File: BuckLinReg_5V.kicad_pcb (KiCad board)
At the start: 2 copper layers, 96 x 56 mm, 41 parts, among them J1 Barrel_Jack, J2 Conn_01x02_Male, J3 Conn_01x02_Male, J4 Conn_01x02_Male, Q1 SQD40061EL, U1 TPS56339DDC, U2 LM1085-5.0

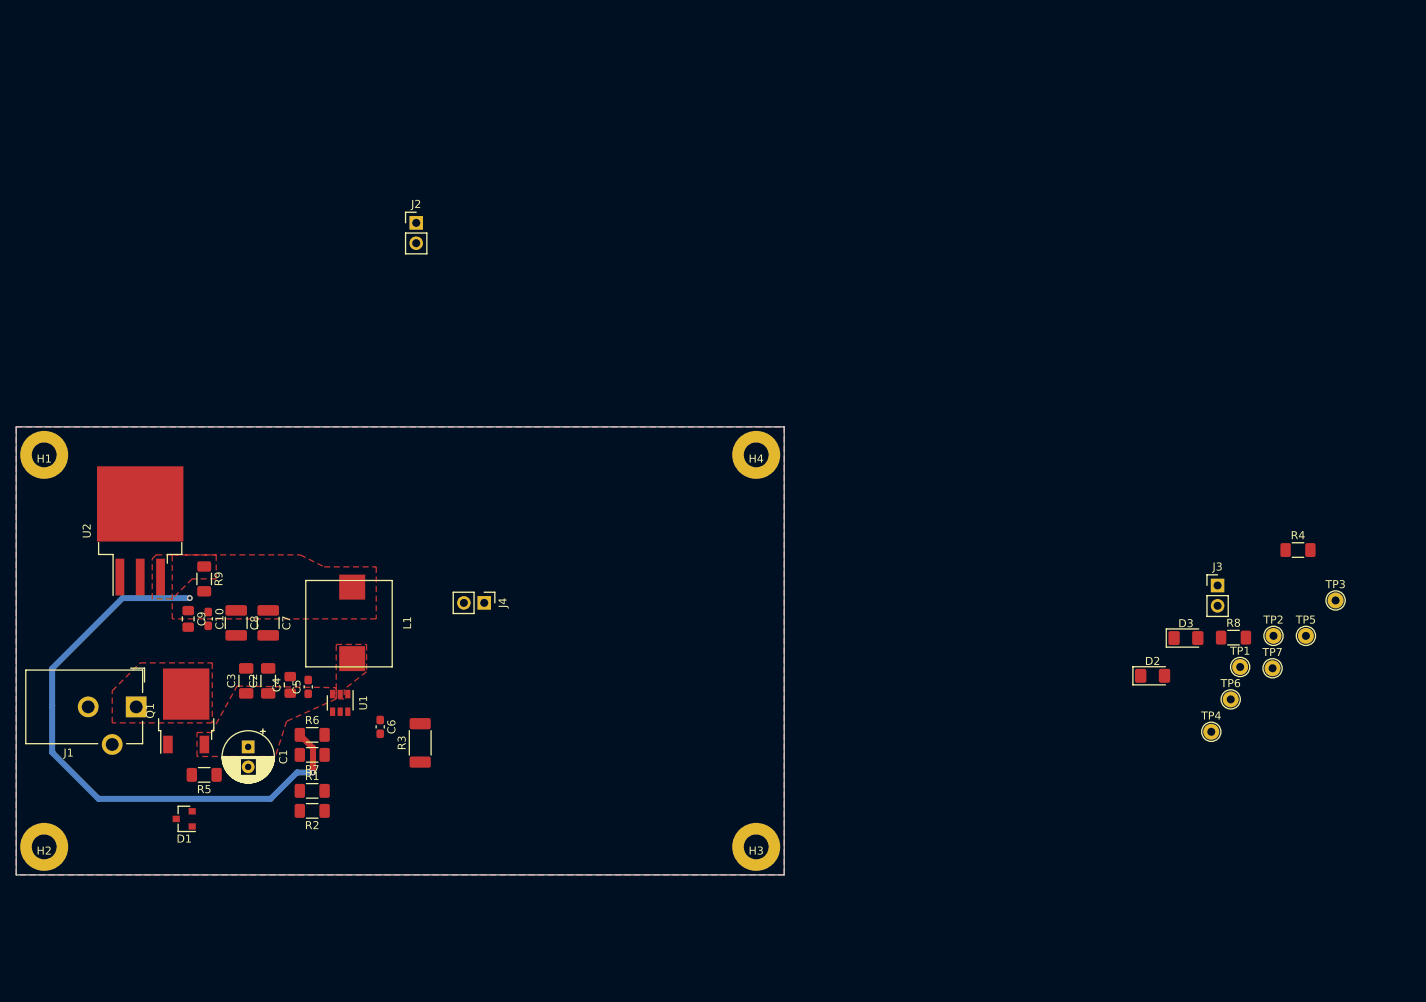
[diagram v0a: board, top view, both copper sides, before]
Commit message: Added overcurrent protection circuit and assigned all MFPNs and footprints
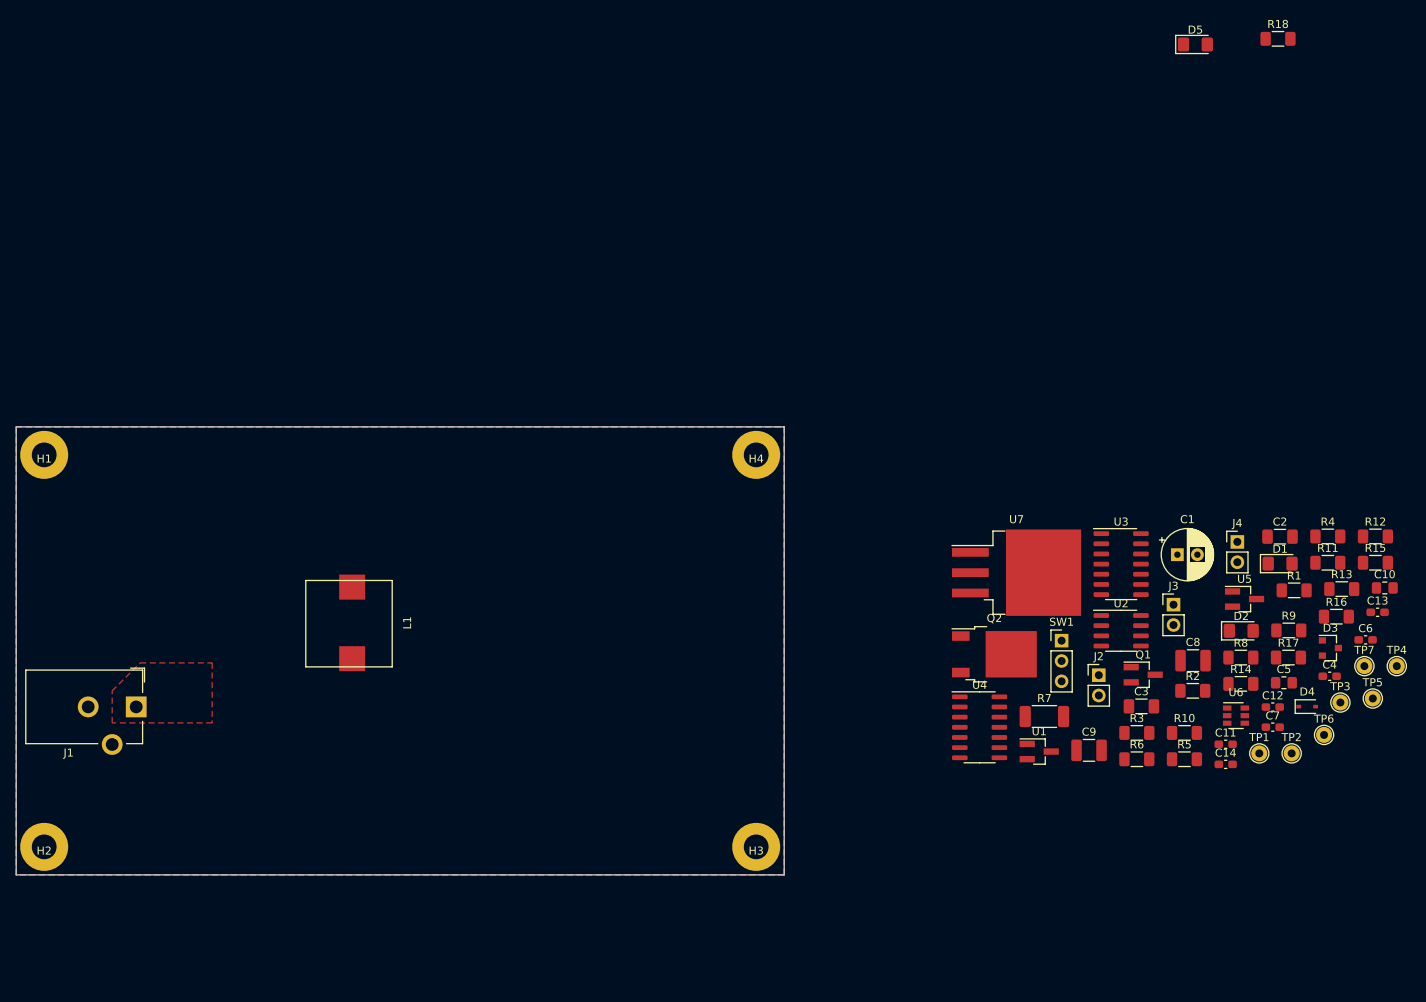
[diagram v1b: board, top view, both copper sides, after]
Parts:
- added C11: 0.1u, Capacitor_SMD:C_0603_1608Metric_Pad1.08x0.95mm_HandSolder, F.Cu at (209.2, 91.7)
- added C12: 0.1u, Capacitor_SMD:C_0603_1608Metric_Pad1.08x0.95mm_HandSolder, F.Cu at (215.1, 87.0)
- added C13: 0.1u, Capacitor_SMD:C_0603_1608Metric_Pad1.08x0.95mm_HandSolder, F.Cu at (228.2, 75.2)
- added C14: 0.1u, Capacitor_SMD:C_0603_1608Metric_Pad1.08x0.95mm_HandSolder, F.Cu at (209.2, 94.2)
- added D4: 3.0, Diode_SMD:D_SOD-323, F.Cu at (219.4, 87.0)
- added D5: YELLOW, Diode_SMD:D_1206_3216Metric_Pad1.42x1.75mm_HandSolder, F.Cu at (205.4, 4.20)
- added Q2: SQD40061EL, Package_TO_SOT_SMD:TO-252-2, F.Cu at (180.3, 80.4)
- added R10: 10k, Resistor_SMD:R_1206_3216Metric_Pad1.30x1.75mm_HandSolder, F.Cu at (204.0, 90.3)
- added R11: 1k, Resistor_SMD:R_1206_3216Metric_Pad1.30x1.75mm_HandSolder, F.Cu at (222.0, 69.0)
- added R12: 1k, Resistor_SMD:R_1206_3216Metric_Pad1.30x1.75mm_HandSolder, F.Cu at (227.9, 65.7)
- added R13: 100k, Resistor_SMD:R_1206_3216Metric_Pad1.30x1.75mm_HandSolder, F.Cu at (223.7, 72.3)
- added R14: 100k, Resistor_SMD:R_1206_3216Metric_Pad1.30x1.75mm_HandSolder, F.Cu at (211.1, 84.1)
- added R15: 10m, Resistor_SMD:R_1206_3216Metric_Pad1.30x1.75mm_HandSolder, F.Cu at (227.9, 69.0)
- added R16: 100k, Resistor_SMD:R_1206_3216Metric_Pad1.30x1.75mm_HandSolder, F.Cu at (223.0, 75.7)
- added R17: 12k, Resistor_SMD:R_1206_3216Metric_Pad1.30x1.75mm_HandSolder, F.Cu at (217.0, 80.8)
- added R18: 10k, Resistor_SMD:R_1206_3216Metric_Pad1.30x1.75mm_HandSolder, F.Cu at (215.7, 3.50)
- added SW1: SW_SPDT, Connector_PinHeader_2.54mm:PinHeader_1x03_P2.54mm_Vertical, F.Cu at (188.7, 78.7)
- added U3: 74HCT00, Package_SO:SOIC-14_3.9x8.7mm_P1.27mm, F.Cu at (196.1, 69.2)
- added U4: SN74HCT02, Package_SO:SOIC-14_3.9x8.7mm_P1.27mm, F.Cu at (178.4, 89.6)
- added U5: TCM810, Package_TO_SOT_SMD:SOT-23_Handsoldering, F.Cu at (211.5, 73.5)
- added U6: TPS56339DDC, Package_TO_SOT_SMD:SOT-23-6, F.Cu at (210.5, 88.1)
- added U7: LM1084-5.0, Package_TO_SOT_SMD:TO-263-3_TabPin2, F.Cu at (183.0, 70.2)
- C10, C5: footprint Capacitor_SMD:C_0603_1608Metric_Pad1.08x0.95mm_HandSolder -> Capacitor_SMD:C_0805_2012Metric_Pad1.18x1.45mm_HandSolder
- C4: footprint Capacitor_SMD:C_0805_2012Metric_Pad1.18x1.45mm_HandSolder -> Capacitor_SMD:C_0603_1608Metric_Pad1.08x0.95mm_HandSolder
- C7: value 10u -> 0.1u; footprint Capacitor_SMD:C_1210_3225Metric_Pad1.33x2.70mm_HandSolder -> Capacitor_SMD:C_0603_1608Metric_Pad1.08x0.95mm_HandSolder
- C9: value 0.1u -> 10u; footprint Capacitor_SMD:C_0805_2012Metric_Pad1.18x1.45mm_HandSolder -> Capacitor_SMD:C_1210_3225Metric_Pad1.33x2.70mm_HandSolder
- D1: value 10V -> GREEN; footprint Diode_SMD:D_SOT-23_ANK -> Diode_SMD:D_1206_3216Metric_Pad1.42x1.75mm_HandSolder
- D3: value GREEN -> 10V; footprint Diode_SMD:D_1206_3216Metric_Pad1.42x1.75mm_HandSolder -> Diode_SMD:D_SOT-23_ANK
- J2, J3, J4: value Conn_01x02_Male -> 1x2 Male
- Q1: value SQD40061EL -> PMBT2222; footprint Package_TO_SOT_SMD:TO-252-2 -> Package_TO_SOT_SMD:SOT-23_Handsoldering
- R1: value 22.1k -> 10k
- R2: value 3.6k -> 10k
- R3: value 30 -> 22.1k; footprint Resistor_SMD:R_2010_5025Metric_Pad1.40x2.65mm_HandSolder -> Resistor_SMD:R_1206_3216Metric_Pad1.30x1.75mm_HandSolder
- R4: value 10k -> 3.6k
- R6: value 36k -> 10k
- R7: value 4.7k -> 30; footprint Resistor_SMD:R_1206_3216Metric_Pad1.30x1.75mm_HandSolder -> Resistor_SMD:R_2010_5025Metric_Pad1.40x2.65mm_HandSolder
- R8: value 10k -> 68k
- R9: value 10m -> 33k
- TP1: value Vin -> U1Vin
- TP2: value U1Vin -> EN
- TP3: value EN -> Vin
- U1: value TPS56339DDC -> TLV76050DBZT; footprint Package_TO_SOT_SMD:SOT-23-6 -> Package_TO_SOT_SMD:SOT-23_Handsoldering
- U2: value LM1085-5.0 -> LMV358; footprint Package_TO_SOT_SMD:TO-263-3_TabPin2 -> Package_SO:SOIC-8_3.9x4.9mm_P1.27mm
- moved C10 147.1 mm to (229.1, 72.1), turned to 0 degrees
- moved D1 140.7 mm to (216.0, 69.1), turned to 0 degrees
- moved R9 135.7 mm to (217.1, 77.4), turned to 0 degrees
- moved C4 129.9 mm to (222.2, 83.2), turned to 0 degrees
- moved C2 127.8 mm to (216.0, 65.7), turned to 0 degrees
- moved C7 126.2 mm to (215.1, 89.5), turned to 0 degrees
- moved R1 125.3 mm to (217.7, 72.4)
- moved C6 123.7 mm to (226.7, 78.6), turned to 0 degrees
- moved U2 123.2 mm to (196.1, 77.5), turned to 0 degrees
- moved R5 122.6 mm to (204.0, 93.5), turned to 0 degrees
- moved C5 122.0 mm to (216.5, 84.0), turned to 0 degrees
- moved Q1 119.7 mm to (198.9, 83.0), turned to 0 degrees
- moved C8 119.7 mm to (205.1, 81.2), turned to 0 degrees
- moved C1 118.6 mm to (203.2, 68.0), turned to 0 degrees
- moved C9 113.8 mm to (192.1, 92.4), turned to 0 degrees
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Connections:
- C1 pad 1: /U1Vin -> /+Vin
- C10 pad 1: /CapNode -> /SR+
- C2 pad 1: /U1Vin -> /+Vin
- C3 pad 1: /U1Vin -> /+Vin
- C4 pad 1: /U1Vin -> /5V0_LOGIC
- C5 pad 1: /U1Vin -> /+Vin
- C6 pad 1: /BOOT -> /+Vin
- C6 pad 2: Net-(C6-Pad2) -> GND
- C7 pad 1: /CapNode -> /BOOT
- C7 pad 2: GND -> Net-(C7-Pad2)
- C8 pad 1: /CapNode -> /SR+
- C9 pad 1: /CapNode -> /SR+
- D1 pad 1: /U1Vin -> GND
- D1 pad 2: /PCheckG -> Net-(D1-Pad2)
- D3 pad 1: GND -> /+Vin
- D3 pad 2: Net-(D3-Pad2) -> /PCheckG
- J2 pad 2: /Vout -> /SR+
- J3 pad 1: GND -> /SR-
- J3 pad 2: /CapNode -> /SR+
- J4 pad 1: /U2Vin -> GND
- J4 pad 2: /CapNode -> /5V0_Out
- L1 pad 2: /CapNode -> /SR+
- Q1 pad 1: /PCheckG -> Net-(Q1-Pad1)
- Q1 pad 2: /Vin -> GND
- Q1 pad 3: /U1Vin -> /EN
- R1 pad 1: /U1Vin -> Net-(D1-Pad2)
- R1 pad 2: /EN -> /+Vin
- R2 pad 1: /EN -> /~PWR_EN
- R2 pad 2: GND -> Net-(Q1-Pad1)
- R3 pad 1: Net-(C6-Pad2) -> /+Vin
- R3 pad 2: /SW -> /EN
- R4 pad 1: Net-(D2-Pad2) -> /EN
- R5 pad 1: /PCheckG -> Net-(D2-Pad2)
- R6 pad 1: /CapNode -> /PCheckG
- R6 pad 2: /FB -> GND
- R7 pad 1: /FB -> Net-(C7-Pad2)
- R7 pad 2: GND -> /SW
- R8 pad 1: Net-(D3-Pad2) -> /SR+
- R8 pad 2: /U1Vin -> /FB
- R9 pad 1: /U2Vin -> /FB
- R9 pad 2: /CapNode -> GND
- TP1 pad 1: /Vin -> /+Vin
- TP2 pad 1: /U1Vin -> /EN
- TP3 pad 1: /EN -> /Vin
- TP7 pad 1: /CapNode -> /SR+
- U1 pad 1: GND -> /5V0_LOGIC
- U1 pad 2: /SW -> /+Vin
- U1 pad 3: /U1Vin -> GND
- U2 pad 1: GND -> /Vo
- U2 pad 2: /Vout -> Net-(R11-Pad1)
- U2 pad 3: /U2Vin -> Net-(R12-Pad1)
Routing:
- net /CapNode: track 73.1 -> 0.00 mm, vias 2 -> 0
- removed copper zone on F.Cu, net /CapNode
- removed copper zone on F.Cu, net /SW
- removed copper zone on F.Cu, net /U1Vin
- removed copper zone on F.Cu, net /U2Vin

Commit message: Two grounds: GNDA and pwrGND.  Continued PCB dev.
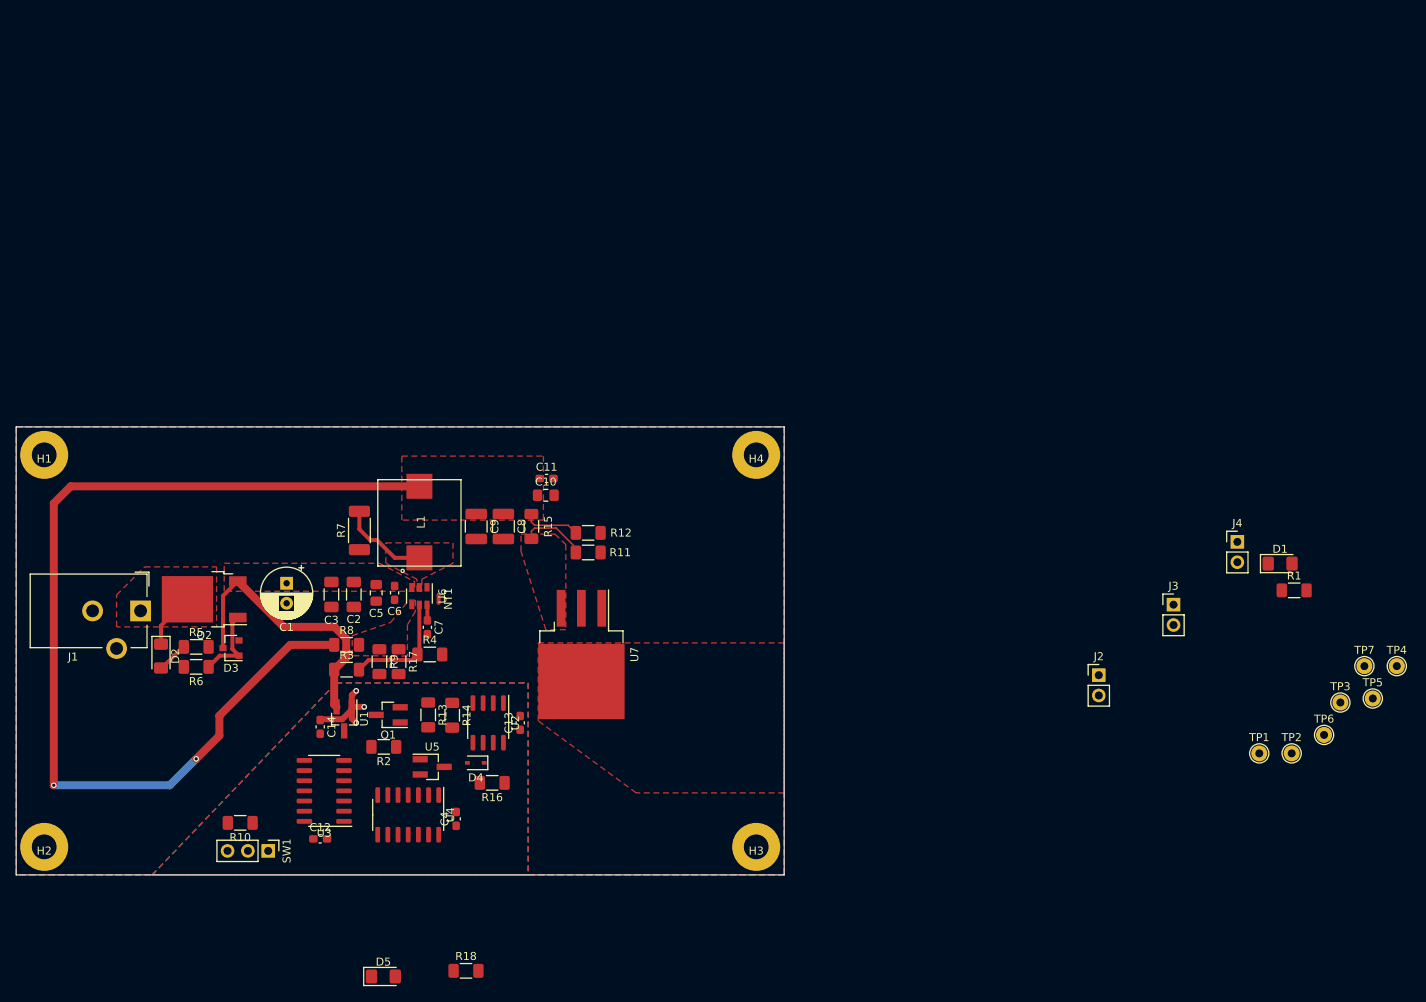
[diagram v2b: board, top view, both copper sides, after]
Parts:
- added NT1: Net-Tie_2, NetTie:NetTie-2_SMD_Pad0.5mm, F.Cu at (110.8, 73.5)
- moved D5 154.5 mm to (103.9, 120.7)
- moved R18 154.5 mm to (114.2, 120.0)
- moved D3 137.4 mm to (84.8, 79.7), turned to 180 degrees
- moved D2 135.1 mm to (76.1, 80.7), turned to 270 degrees
- moved R5 124.3 mm to (80.5, 79.5)
- moved C6 121.5 mm to (105.3, 72.8), turned to 270 degrees
- moved C12 120.2 mm to (96.0, 103.5)
- moved R10 118.6 mm to (86.0, 101.5), turned to 180 degrees
- moved R6 118.2 mm to (80.5, 82.0), turned to 180 degrees
- moved C2 116.0 mm to (100.2, 73.0), turned to 270 degrees
- moved R13 115.3 mm to (109.5, 88.0), turned to 270 degrees
- moved C5 114.0 mm to (103.0, 72.8), turned to 270 degrees
- moved R9 113.7 mm to (103.4, 81.3), turned to 270 degrees
- moved C14 113.3 mm to (96.0, 89.5), turned to 270 degrees
- moved R4 113.2 mm to (109.7, 80.5)
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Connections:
- net Net-(R11-Pad1) renamed /DFA-
- net Net-(R12-Pad1) renamed /DFA+
- C1 pad 2: GND -> GNDPWR
- C10 pad 2: GND -> GNDPWR
- C11 pad 2: GND -> GNDPWR
- C12 pad 2: GND -> GNDA
- C13 pad 2: GND -> GNDA
- C14 pad 2: GND -> GNDA
- C2 pad 2: GND -> GNDPWR
- C3 pad 2: GND -> GNDPWR
- C4 pad 2: GND -> GNDA
- C5 pad 2: GND -> GNDPWR
- C6 pad 2: GND -> GNDPWR
- C8 pad 2: GND -> GNDPWR
- C9 pad 2: GND -> GNDPWR
- D1 pad 1: GND -> GNDPWR
- D4 pad 2: GND -> GNDA
- H1 pad 1: GND -> GNDPWR
- H2 pad 1: GND -> GNDPWR
- H3 pad 1: GND -> GNDPWR
- H4 pad 1: GND -> GNDPWR
- J1 pad 2: GND -> GNDPWR
- J4 pad 1: GND -> GNDPWR
- Q1 pad 2: GND -> GNDA
- R10 pad 2: GND -> GNDA
- R13 pad 2: GND -> GNDA
- R17 pad 2: GND -> GNDA
- R18 pad 2: GND -> GNDPWR
- R4 pad 2: GND -> GNDA
- R5 pad 2: GND -> GNDPWR
- R6 pad 2: GND -> GNDPWR
- R9 pad 2: GND -> GNDA
- SW1 pad 3: GND -> GNDA
- U1 pad 3: GND -> GNDA
- U2 pad 4: GND -> GNDA
- U3 pad 10: GND -> GNDA
- U3 pad 12: GND -> GNDA
- U3 pad 13: GND -> GNDA
- U3 pad 7: GND -> GNDA
- U3 pad 9: GND -> GNDA
- U4 pad 7: GND -> GNDA
- U5 pad 1: GND -> GNDA
- U6 pad 1: GND -> GNDPWR
- U7 pad 1: GND -> GNDPWR
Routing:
- net /SR+: track 0.00 -> 132.7 mm, vias 0 -> 2
- net /+Vin: track 0.00 -> 34.9 mm
- net /EN: track 0.00 -> 14.4 mm
- net /SW: track 0.00 -> 11.2 mm
- net /5V0_LOGIC: track 0.00 -> 10.8 mm, vias 0 -> 3
- net /PCheckG: track 0.00 -> 9.77 mm
- net /SR-: track 0.00 -> 8.28 mm
- net /Vin: track 0.00 -> 6.98 mm
- net Net-(D2-Pad2): track 0.00 -> 3.94 mm
- net /BOOT: track 0.00 -> 1.96 mm
- added copper zone on F.Cu, net /+Vin
- added copper zone on B.Cu, net /5V0_LOGIC
- added copper zone on F.Cu, net /5V0_Out
- added copper zone on F.Cu, net /FB
- added copper zone on F.Cu, net /SR+
- added copper zone on F.Cu, net /SR-
- added copper zone on F.Cu, net /SW
- added copper zone on F.Cu, net GNDA
- added copper zone on B.Cu, net GNDPWR
- added copper zone on F.Cu, net GNDPWR
- removed copper zone on B.Cu, net GND
- removed copper zone on F.Cu, net GND

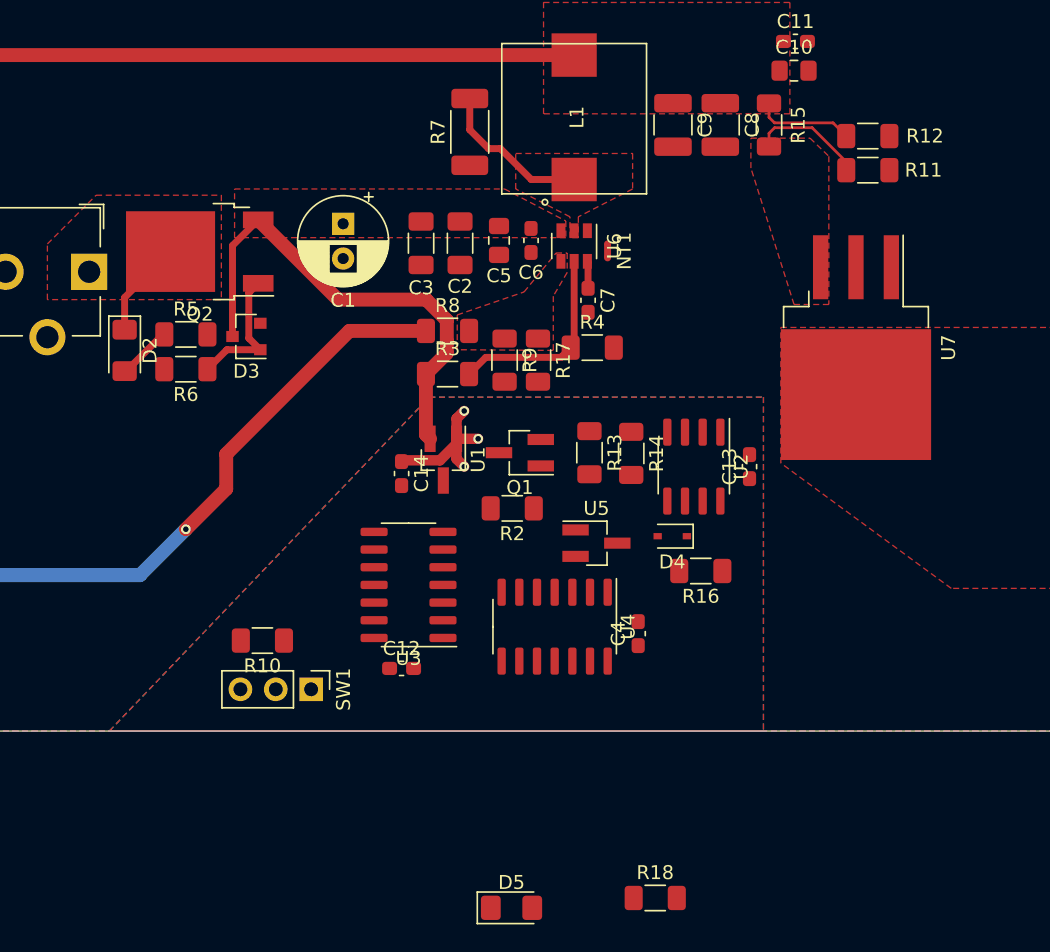
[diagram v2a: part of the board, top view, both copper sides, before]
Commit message: Simulated zener for different values R.  Routed logic portion of board.
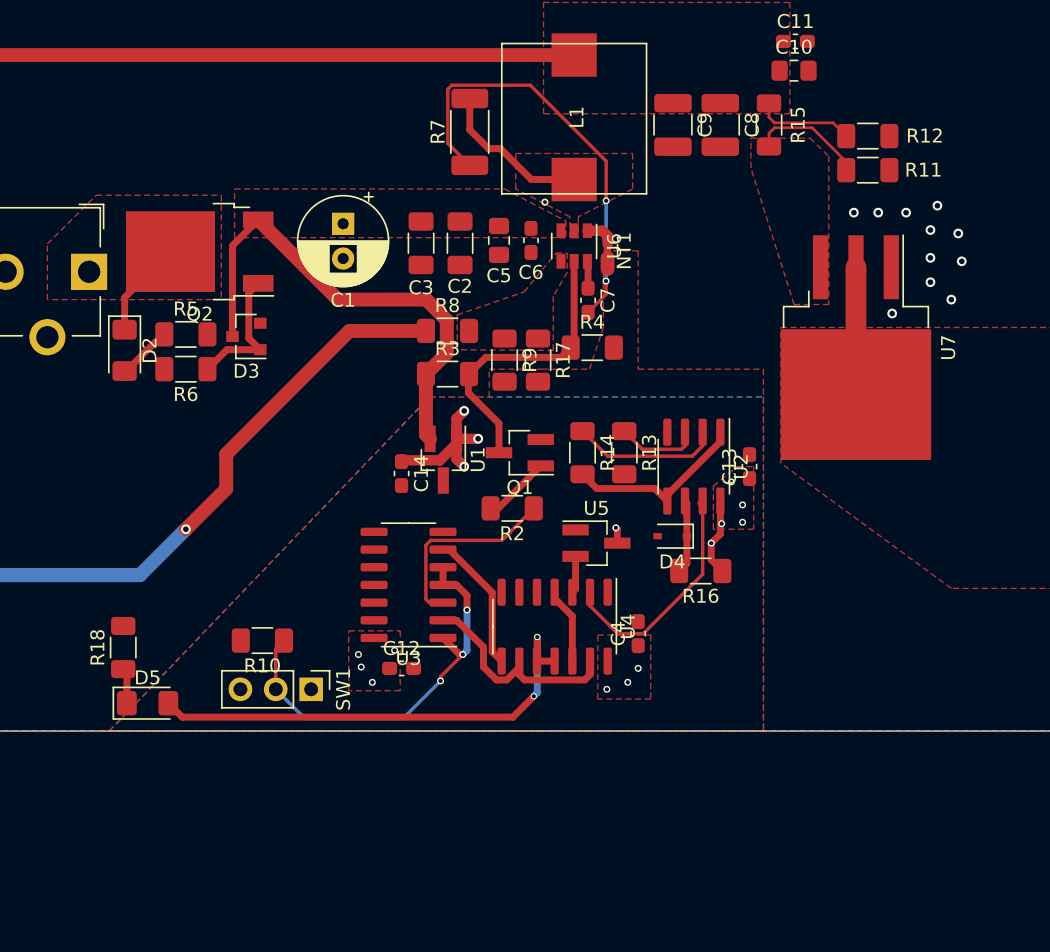
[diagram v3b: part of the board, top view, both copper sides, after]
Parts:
- R16: value 100k -> 10k
- moved R18 42.2 mm to (76.0, 102.0), turned to 90 degrees
- moved D5 30.0 mm to (77.8, 106.0)
- moved R14 3.50 mm to (109.0, 88.0)
- moved R13 2.50 mm to (112.0, 88.0)
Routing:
- net /Q: track 0.00 -> 34.7 mm, vias 0 -> 2
- net Net-(C7-Pad2): track 0.00 -> 31.3 mm, vias 0 -> 2
- net /SW_SIG: track 0.00 -> 29.7 mm, vias 0 -> 3
- net /OCP_TRIGGER: track 0.00 -> 17.1 mm
- net /~Q: track 0.00 -> 16.3 mm
- net /~PWR_EN: track 0.00 -> 14.1 mm
- net /Vo: track 0.00 -> 13.4 mm
- net /DFA-: track 0.00 -> 10.7 mm
- net /~SW_SIG: track 0.00 -> 10.0 mm
- net /5V0_Out: track 0.00 -> 9.15 mm
- net /5V0_LOGIC: track 10.8 -> 17.6 mm, vias 3 -> 16
- net /EN: track 14.4 -> 21.0 mm
- net /DFA+: track 0.00 -> 5.98 mm
- net /S: track 0.00 -> 5.48 mm
- net Net-(D4-Pad1): track 0.00 -> 5.31 mm
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- added copper zone on F.Cu, net /5V0_LOGIC
